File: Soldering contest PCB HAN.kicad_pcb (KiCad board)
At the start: 2 copper layers, 99.1 x 98.6 mm, 18 parts, among them J1 Screw_Terminal_01x02, Q1 2N3904, Q2 2N3904

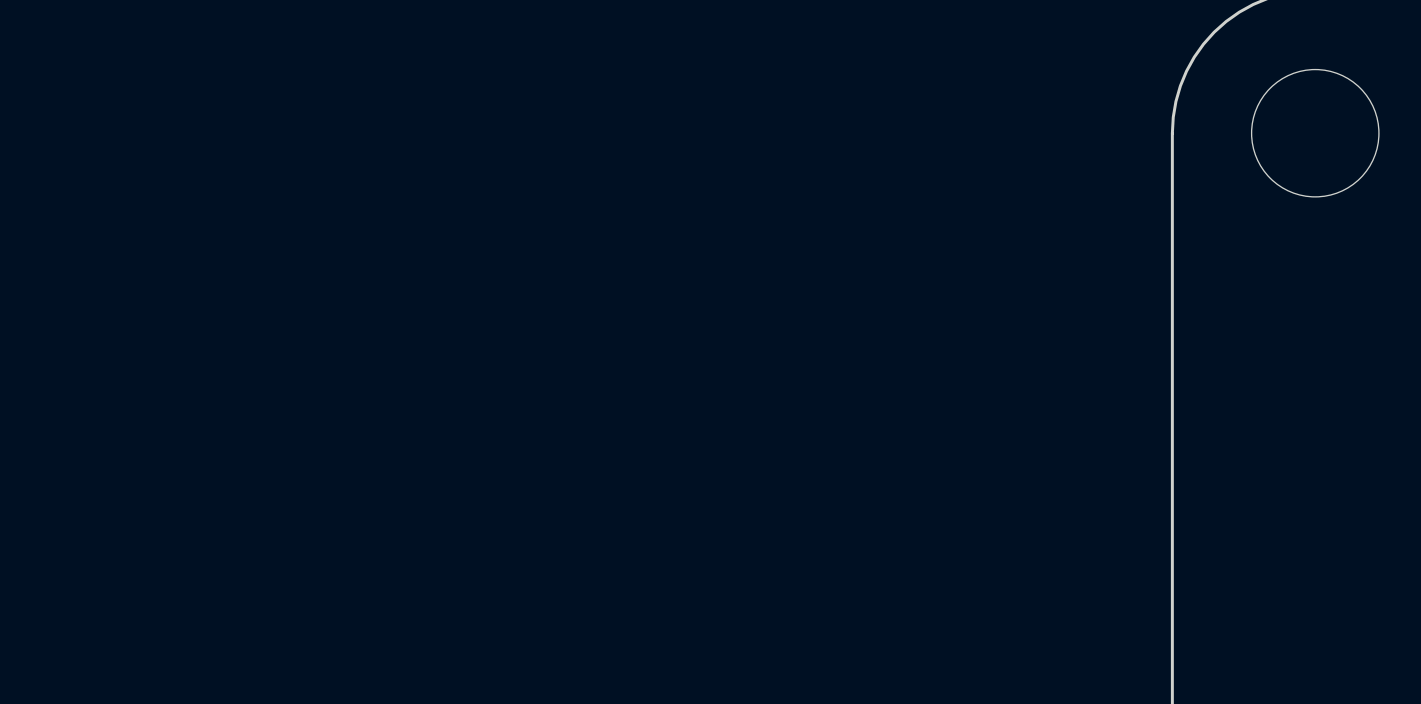
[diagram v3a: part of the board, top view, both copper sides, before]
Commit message: added todo list
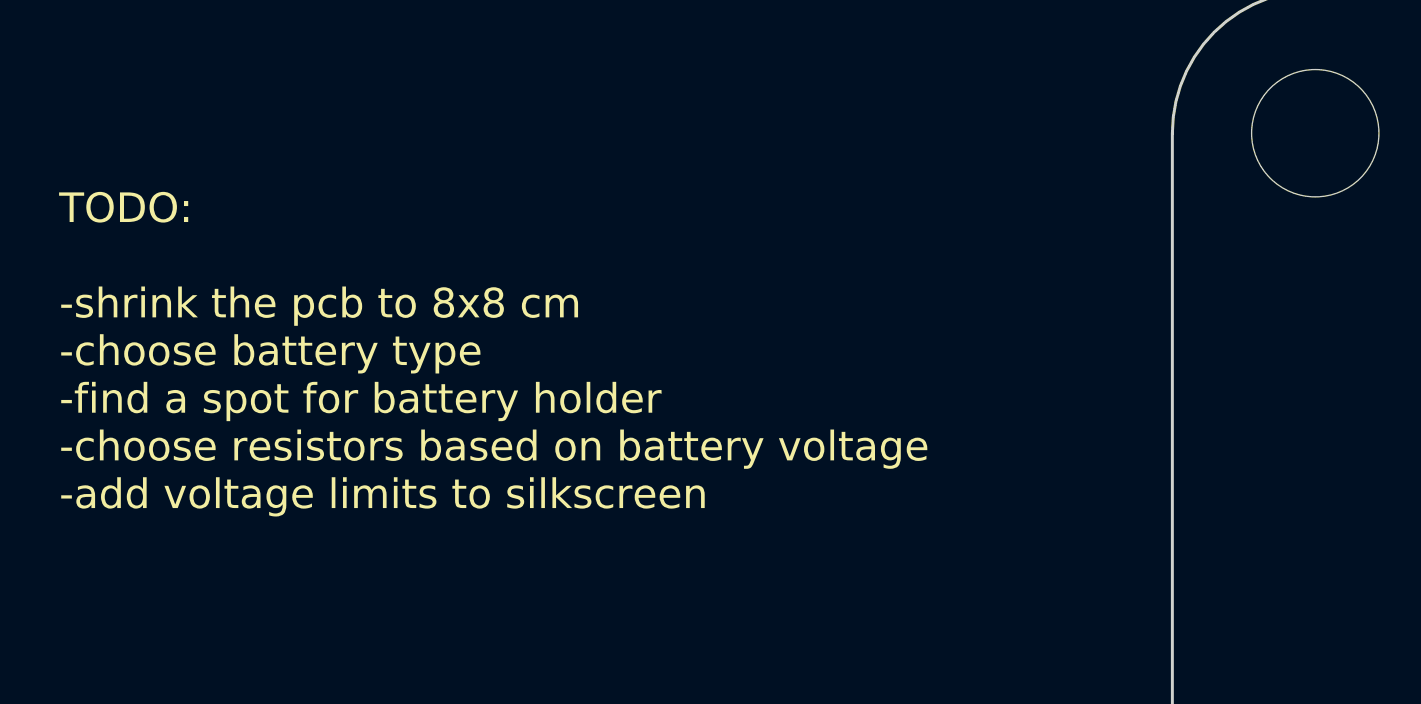
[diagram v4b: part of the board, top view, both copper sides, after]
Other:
- board text added: "TODO: -shrink the pcb to 8x8 cm -choose battery type -find a spot for battery holder -choose resistors based on battery voltage -add voltage limits to silkscreen"
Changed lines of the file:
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@@
     (effects (font (size 1 1) (thickness 0.15)))
+  )
+  (gr_text "TODO:\n\n-shrink the pcb to 8x8 cm\n-choose battery type\n-find a spot for battery holder\n-choose resistors based on battery voltage\n-add voltage limits to silkscreen" (at 73.66 63.5) (layer "F.SilkS")
+    (effects (font (size 1 1) (thickness 0.15)) (justify left))
   )
   (segment (start 143 97.052) (end 139.7 97.052) (width 0.3) (layer "F.Cu") (net 1))

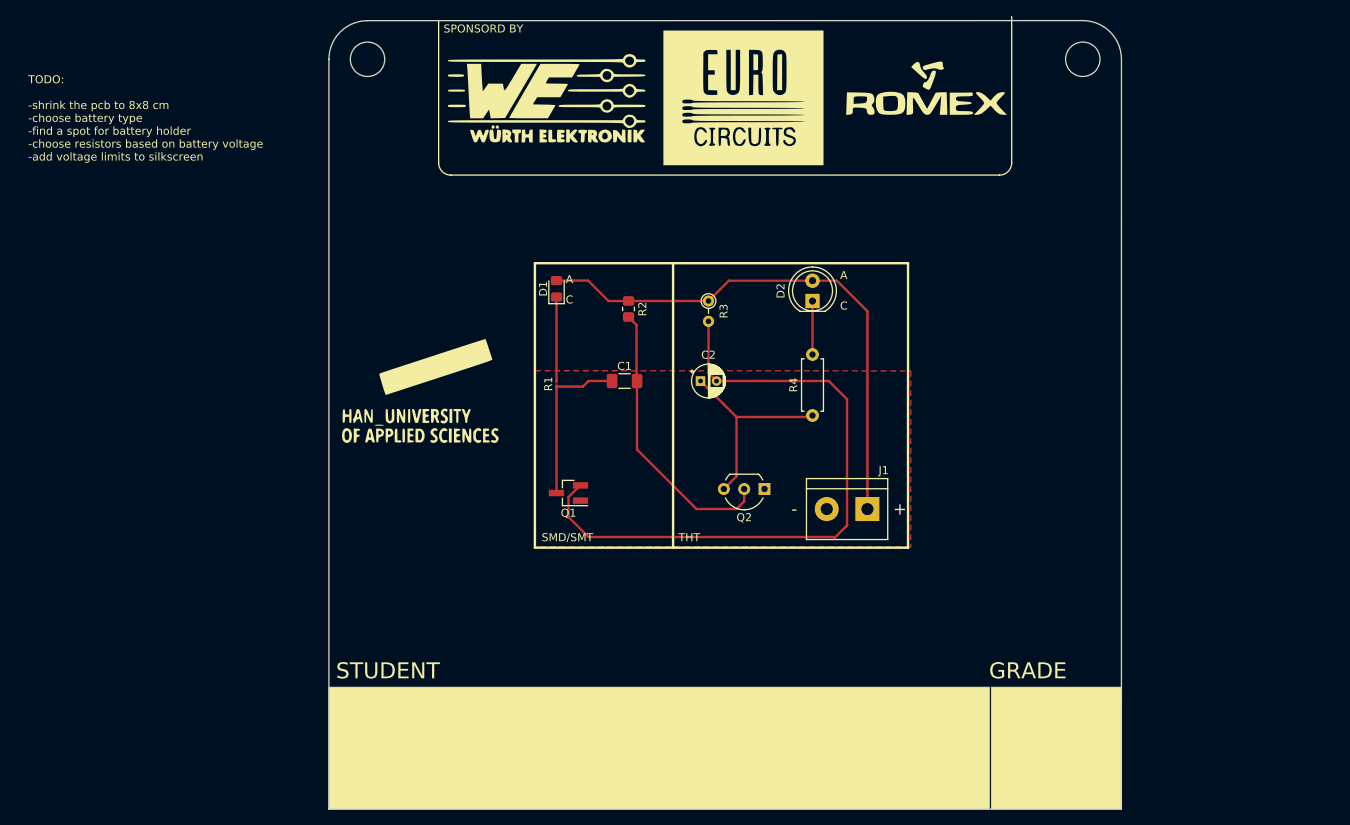
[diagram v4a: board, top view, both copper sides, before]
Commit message: add bat, switch changed schematic
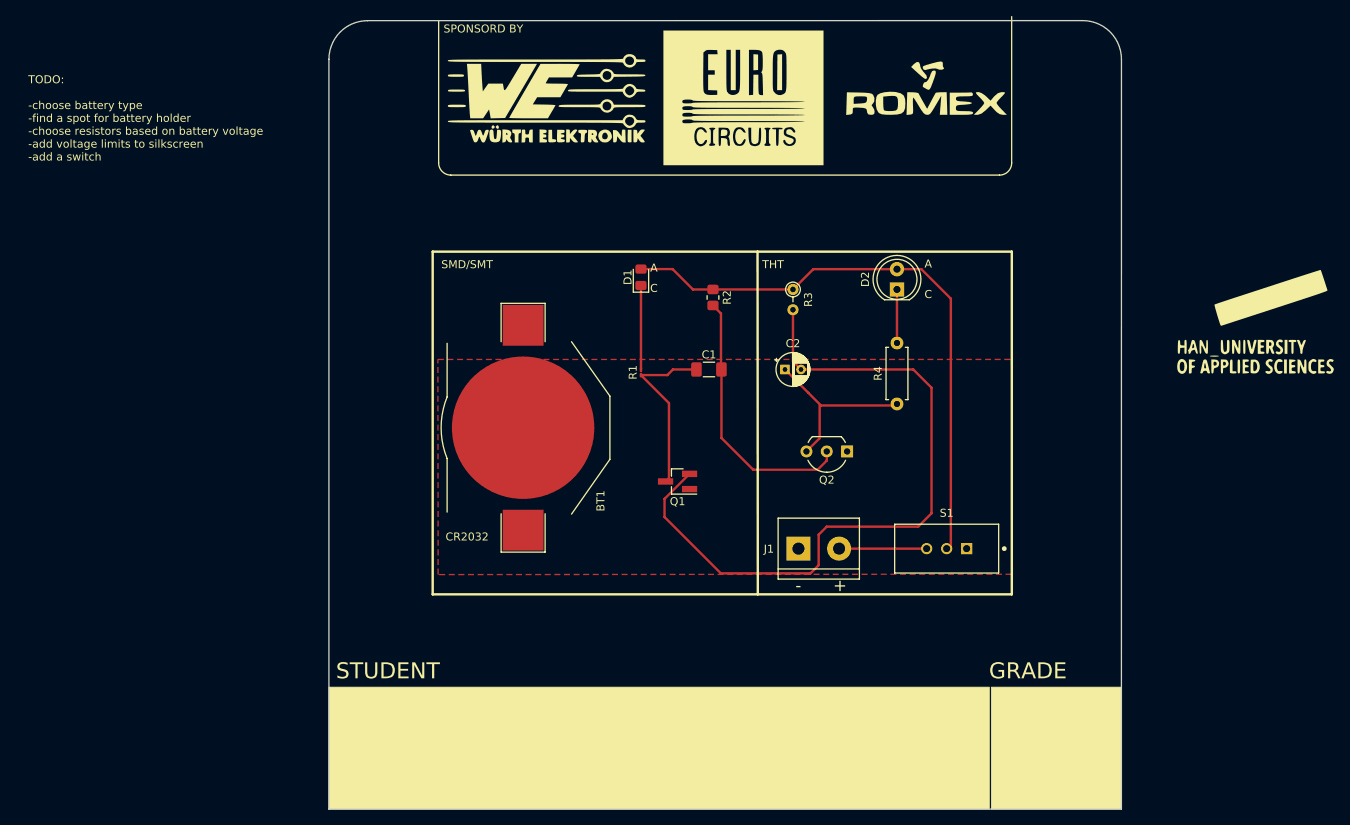
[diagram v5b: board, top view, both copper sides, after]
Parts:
- removed REF** (x2): MountingHole_4.3mm_M4, MountingHole:MountingHole_4.3mm_M4
- added BT1: BATTERY-6.8MM_SMD, Battery:BatteryHolder_Keystone_3002_1x2032, F.Cu at (135.5, 102.2)
- added S1: SWITCH-SPDT-PTH-11.6X4.0MM-KIT, SnapEDA Library:SW_1825159-1, F.Cu at (188.5, 117.3)
- moved G*** 104.8 mm to (227.1, 88.9)
- moved Q1 13.7 mm to (154.8, 108.9)
- moved Q2 11.3 mm to (176.0, 105.2)
- moved C1 10.7 mm to (158.8, 94.9)
- moved C2 10.7 mm to (168.3, 94.9)
- moved D2 10.7 mm to (182.3, 84.9)
- moved R1 10.7 mm to (150.3, 95.3)
- moved R2 10.7 mm to (159.3, 85.9)
- moved R3 10.7 mm to (169.3, 84.9)
- moved R4 10.7 mm to (182.3, 99.2)
- moved D1 10.7 mm to (150.3, 83.4)
- moved J1 9.94 mm to (169.9, 117.3), turned to 0 degrees
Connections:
- J1 pad 1: Net-(D1-Pad2) -> GND
- J1 pad 2: GND -> Net-(J1-Pad2)
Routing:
- net Net-(J1-Pad2): track 0.00 -> 10.9 mm
- net Net-(C2-Pad2): track 82.0 -> 89.2 mm
- net Net-(D1-Pad2): track 67.3 -> 73.6 mm
- net Net-(C2-Pad1): track 25.6 -> 22.3 mm
- net Net-(C1-Pad2): track 35.4 -> 33.4 mm
- net Net-(C1-Pad1): track 20.5 -> 22.2 mm
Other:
- board text added: "CR2032"
- board text added: "D1"
- board text added: "J1"
- board text added: "TODO: -choose battery type -find a spot for battery holder -choose resistors based on battery voltage -add voltage limits to silkscreen -add a switch"
- board text added: "←•→"
- board text removed: "TODO: -shrink the pcb to 8x8 cm -choose battery type -find a spot for battery holder -choose resistors based on battery voltage -add voltage limits to silkscreen"

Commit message: improved wiring and connected everything
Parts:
- BT1: value BATTERY-6.8MM_SMD -> Battery_Cell
- moved S1 13.9 mm to (189.2, 103.4), turned to -90 degrees
- moved J1 2.94 mm to (167.0, 117.3)
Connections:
- BT1 pad 1: (no net) -> Net-(S1-Pad1)
- BT1 pad 2: (no net) -> GND
- S1 pad 1: Net-(BT1-Pad+) -> Net-(S1-Pad1)
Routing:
- net Net-(S1-Pad1): track 0.00 -> 112.9 mm
- net Net-(C2-Pad2): track 89.2 -> 63.9 mm
- net Net-(D1-Pad2): track 73.6 -> 59.8 mm
- net Net-(J1-Pad2): track 10.9 -> 22.9 mm
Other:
- board text added: "BT1"
- board text removed: "D1"

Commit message: Working on ERC
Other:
- board text added: "TODO: -choose resistors based on battery voltage -add voltage limits to silkscreen"
- board text removed: "TODO: -choose battery type -find a spot for battery holder -choose resistors based on battery voltage -add voltage limits to silkscreen -add a switch"
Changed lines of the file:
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@@
     (effects (font (size 1 1) (thickness 0.15)))
   )
-  (gr_text "TODO:\n\n-choose battery type\n-find a spot for battery holder\n-choose resistors based on battery voltage\n-add voltage limits to silkscreen\n-add a switch" (at 73.66 63.5) (layer "F.SilkS")
+  (gr_text "TODO:\n\n-choose resistors based on battery voltage\n-add voltage limits to silkscreen\n" (at 73.66 63.5) (layer "F.SilkS")
     (effects (font (size 1 1) (thickness 0.15)) (justify left))
   )

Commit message: archived 3d models
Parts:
- moved G*** 29.9 mm to (201.7, 73.2)
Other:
- board text added: "TODO: -choose resistors based on battery voltage -add voltage limits to silkscreen -add values for components on back of pcb?"
- board text removed: "TODO: -choose resistors based on battery voltage -add voltage limits to silkscreen"
